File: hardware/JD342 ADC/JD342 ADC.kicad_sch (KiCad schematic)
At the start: 12 parts, among them U1 ADS7279IPW, U2 OPA192IDBVR

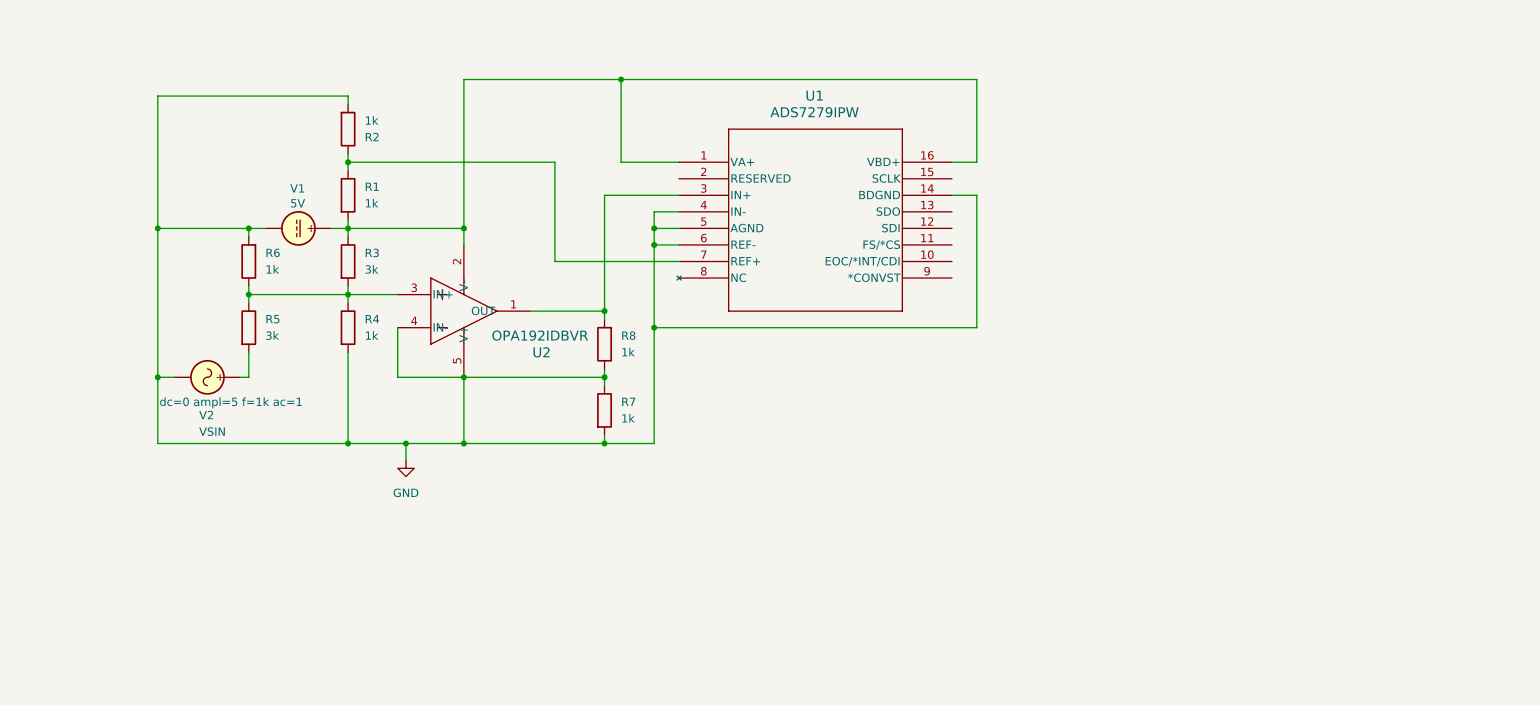
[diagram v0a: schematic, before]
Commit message: fix: JD342 ADC now opens properly
there was an issue with having two kicad_sch files in the directory; replaced the old one w/ the new one & was able to fix it & thereafter view successfully
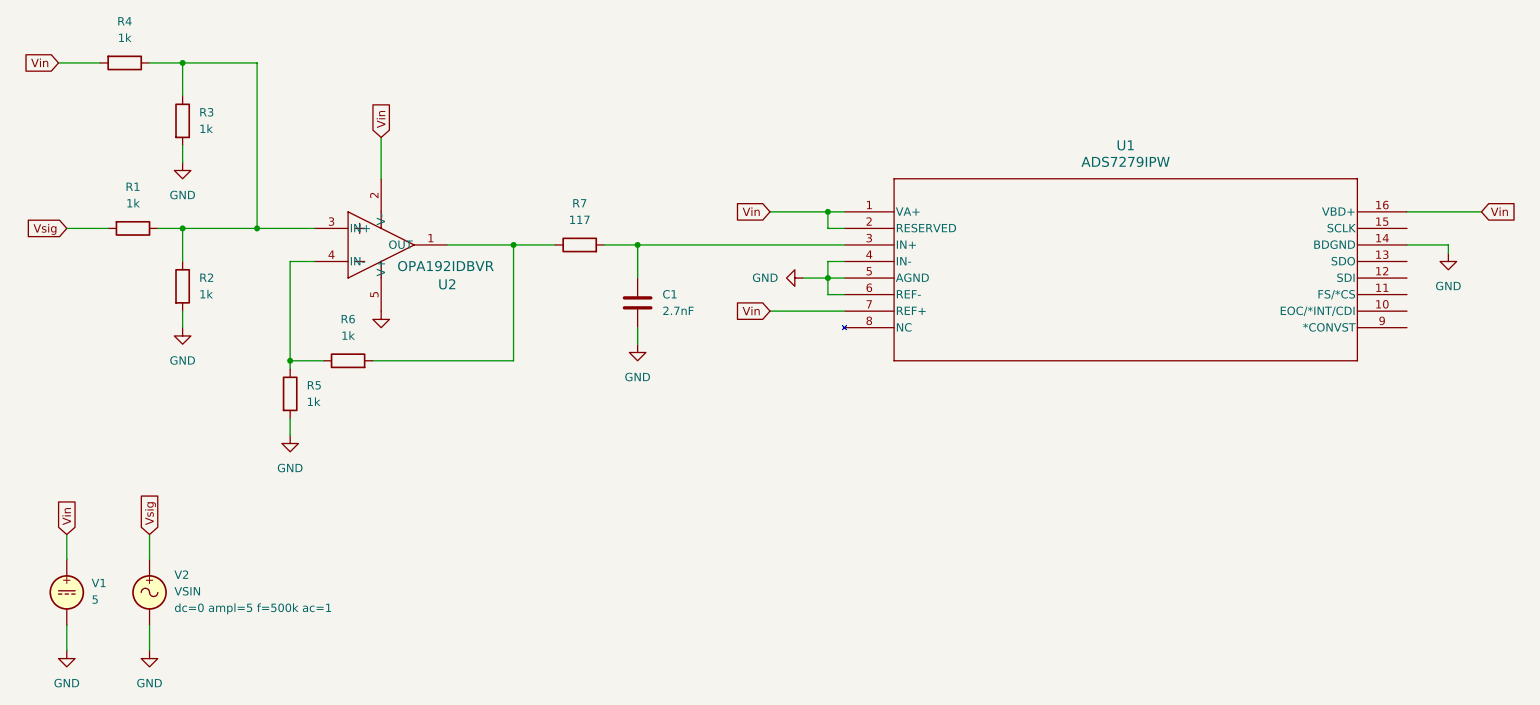
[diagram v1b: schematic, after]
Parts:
- removed R8: 1k, symbol Device:R
- added C1: 2.7nF, symbol Device:C
- R3, R5: value 3k -> 1k
- R7: value 1k -> 117
- V1: value 5V -> 5
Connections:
- net GND: now also R3.2, R5.2, C1.2; no longer R4.2, R6.2, R7.1, R7.2, U2.4 (IN-)
- net Vin: now reaches U1.1 (VA+), U1.16 (VBD+), U2.2 (V-), V1.1
- net Vin: now also R4.2, U1.2 (RESERVED), U1.7 (REF+); no longer R1.2, R3.1
- net at R1.1, R2.1: now also R3.1, R4.1, U2.3 (IN+); no longer U1.7 (REF+)
- net Vsig: now reaches V2.1
- net Vsig: now also R1.2; no longer R5.2
- net at U2.1 (OUT): now also R6.2, R7.1; no longer U1.3 (IN+)
- new net: C1.1, R7.2, U1.3 (IN+)
- new net: R5.1, R6.1, U2.4 (IN-)
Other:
- moved on the sheet: U1, U2, V1, V2
